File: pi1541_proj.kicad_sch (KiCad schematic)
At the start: 15 parts, among them J1 Raspberry_Pi_2_3, J2 DIN-6, SW1 SW_Push, SW2 SW_Push, SW3 SW_Push, SW4 SW_Push, SW5 SW_Push, U1 Level_Converter, U2 7406

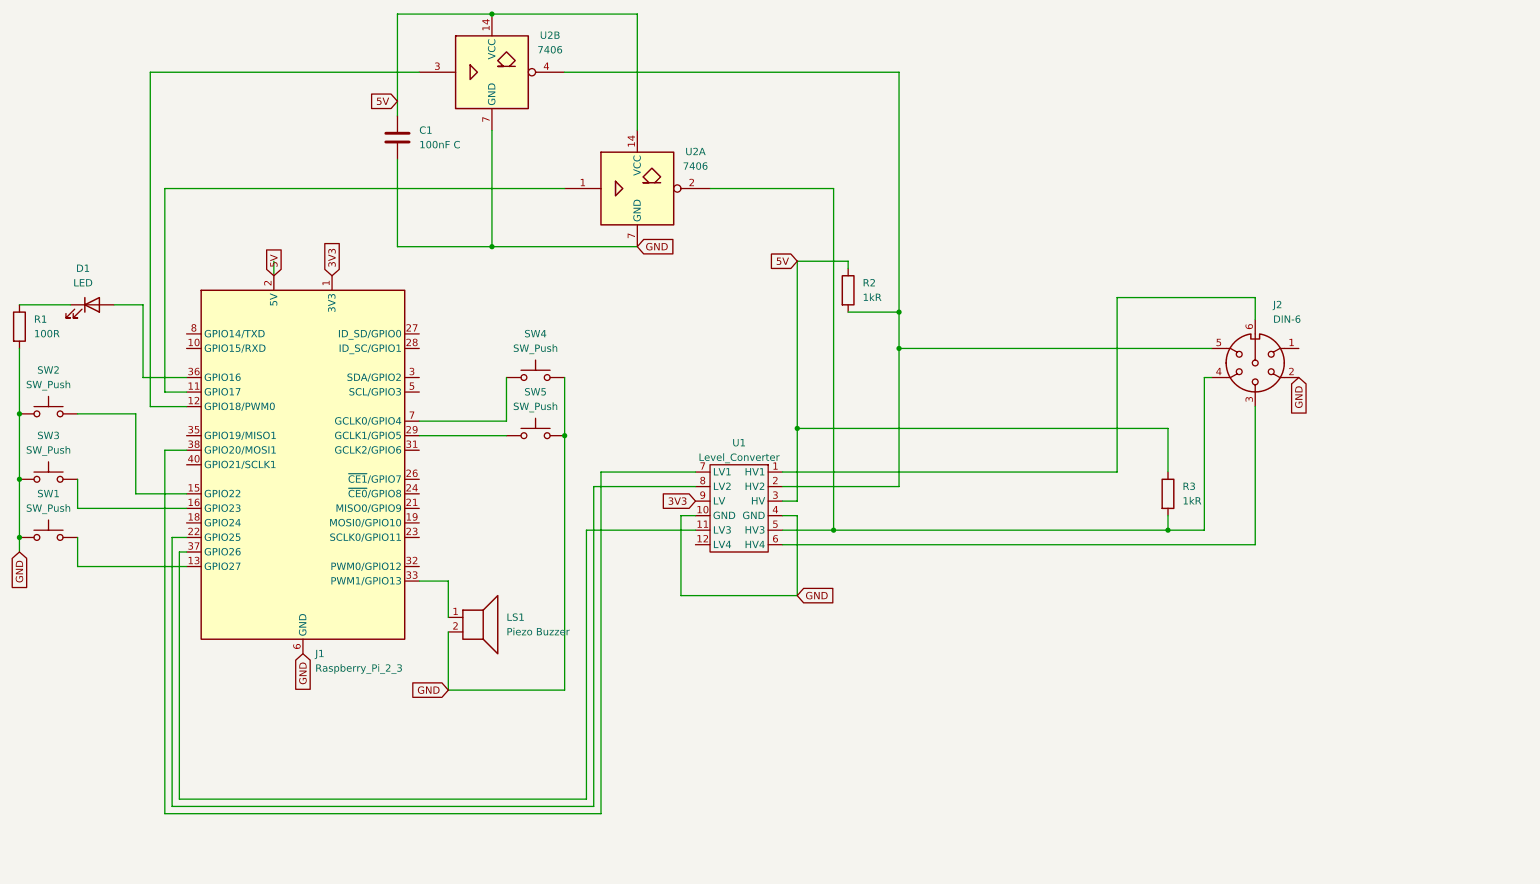
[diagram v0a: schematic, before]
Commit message: Switched for a transistor based invertor and improved schematic
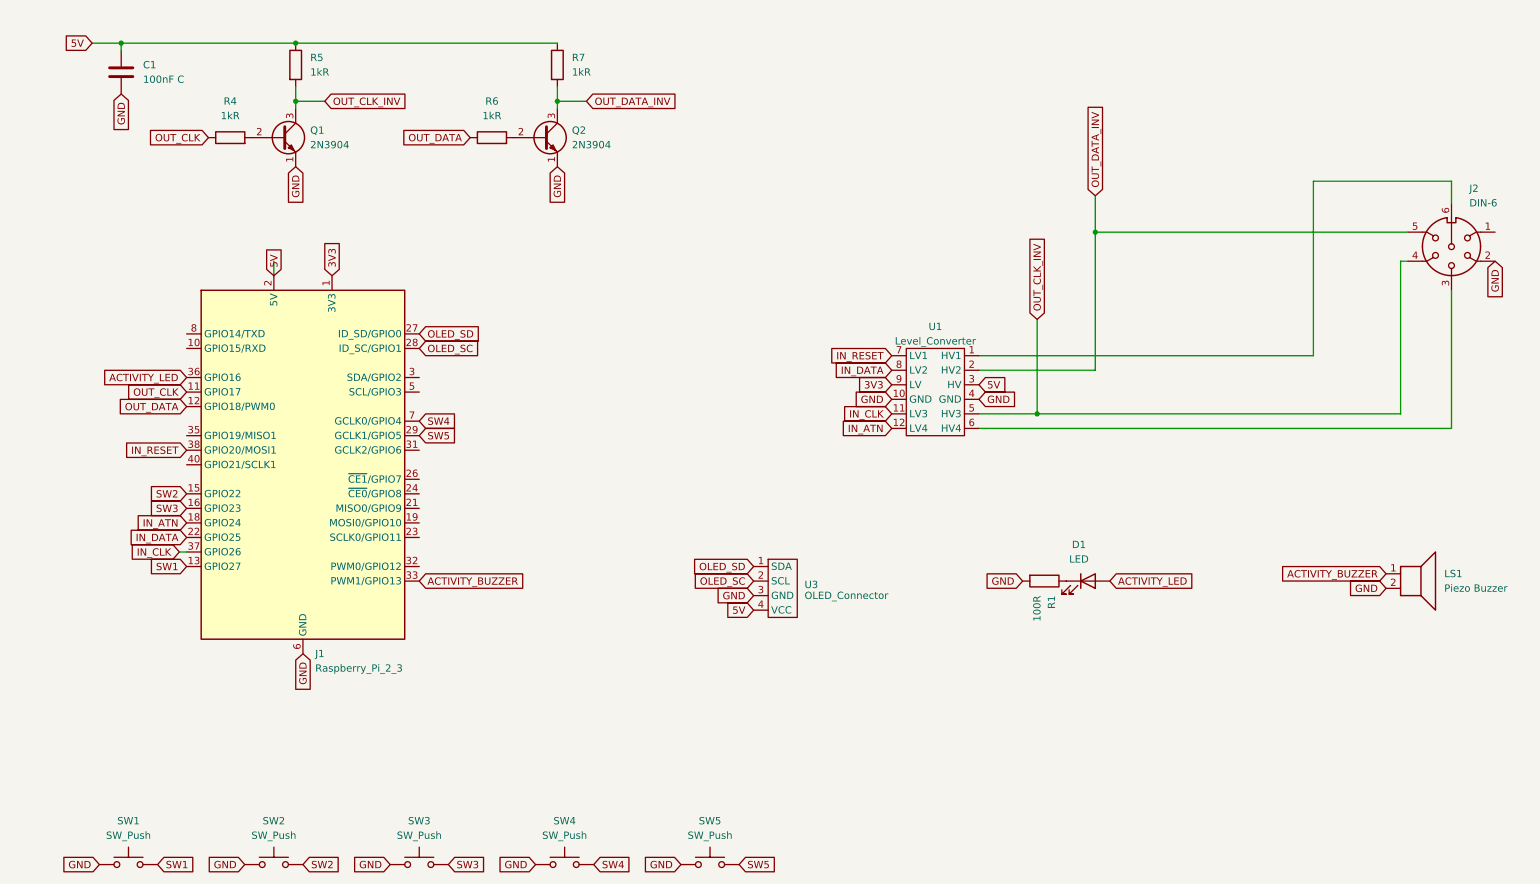
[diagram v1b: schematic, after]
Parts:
- removed R2, R3: 1kR, symbol Device:R
- removed U2: 7406, symbol 74xx_IEEE:7406
- added Q1, Q2: 2N3904, Package_TO_SOT_THT:TO-92_Inline, symbol Transistor_BJT:2N3904
- added R4, R5, R6, R7: 1kR, Resistor_THT:R_Box_L8.4mm_W2.5mm_P5.08mm, symbol Device:R
- added U3: OLED_Connector, Connectors:OLED_Connector, symbol MySymbols:OLED_Display
- C1: footprint (none) -> Capacitor_THT:C_Rect_L4.0mm_W2.5mm_P2.50mm
- D1: footprint (none) -> LED_THT:LED_D3.0mm
- J2: footprint (none) -> Connectors:SDF-J_DIN-6
- LS1: footprint (none) -> Connectors:PS12_Piezo_Buzzer
- R1: footprint (none) -> Resistor_THT:R_Box_L8.4mm_W2.5mm_P5.08mm
- SW1, SW2, SW3, SW4, SW5: footprint (none) -> Button_Switch_Keyboard:SW_Cherry_MX_1.00u_PCB
- U1: footprint (none) -> Connectors:12009 Level Converter
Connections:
- net 5V: now also R5.1, R7.1, U3.4 (VCC)
- net GND: now also SW4.1, SW5.1, Q1.1 (E), Q2.1 (E), U3.3 (GND); no longer SW4.2, SW5.2
- net OUT_CLK: now reaches J1.11 (GPIO17)
- net OUT_CLK: now also R4.1
- net OUT_DATA: now reaches J1.12 (GPIO18/PWM0)
- net OUT_DATA: now also R6.1
- net SW1: now reaches J1.13 (GPIO27), SW1.2
- net SW2: now reaches J1.15 (GPIO22), SW2.2
- net SW3: now reaches J1.16 (GPIO23), SW3.2
- net IN_ATN: now reaches J1.18 (GPIO24)
- net IN_ATN: now also U1.12 (LV4)
- net IN_DATA: now reaches J1.22 (GPIO25), U1.8 (LV2)
- net OLED_SD: now reaches J1.27 (ID_SD/GPIO0)
- net OLED_SD: now also U3.1 (SDA)
- net OLED_SC: now reaches J1.28 (ID_SC/GPIO1)
- net OLED_SC: now also U3.2 (SCL)
- net SW5: now reaches J1.29 (GCLK1/GPIO5)
- net SW5: now also SW5.2; no longer SW5.1
- net ACTIVITY_BUZZER: now reaches J1.33 (PWM1/GPIO13), LS1.1
- net ACTIVITY_LED: now reaches D1.2 (A), J1.36 (GPIO16)
- net IN_CLK: now reaches J1.37 (GPIO26), U1.11 (LV3)
- net IN_RESET: now reaches J1.38 (GPIO20/MOSI1), U1.7 (LV1)
- net SW4: now reaches J1.7 (GCLK0/GPIO4)
- net SW4: now also SW4.2; no longer SW4.1
- net OUT_CLK_INV: now reaches J2.4, U1.5 (HV3)
- net OUT_CLK_INV: now also Q1.3 (C), R5.2
- net OUT_DATA_INV: now reaches J2.5, U1.2 (HV2)
- net OUT_DATA_INV: now also Q2.3 (C), R7.2
- new net: Q1.2 (B), R4.2
- new net: Q2.2 (B), R6.2
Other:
- moved on the sheet: C1, D1, J2, LS1, R1, SW1, SW2, SW3, SW4, SW5, U1
